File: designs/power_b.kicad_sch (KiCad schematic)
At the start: 30 parts, among them J10 1P2, J11 1P0, J12 GND, J7 3P3, J8 1P8, J9 1P0, U3 TPS82085SIL, U4 MAX1589AETT100T, U5 MIC47050-1.2YML, U6 TPS82085SIL

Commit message: Add files via upload
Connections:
- net +3V3: no longer C52.1, U3.1 (EN), U3.3 (VIN), U3.4 (VIN)
- new net: C52.1, U3.1 (EN), U3.3 (VIN), U3.4 (VIN)
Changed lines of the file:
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@@
 		(lib_id "PicoEVB-rescue:CP")
 		(at 215.9 43.18 0)
+		(mirror y)
 		(unit 1)
 		(exclude_from_sim no)
@@
 		(dnp no)
 		(property "Reference" "C62"
-			(at 216.535 40.64 0)
+			(at 215.265 40.64 0)
 			(effects
 				(font
@@
 		)
 		(property "Value" "100uf"
-			(at 216.535 45.72 0)
+			(at 215.265 45.72 0)
 			(effects
 				(font
@@
 		)
 		(property "Footprint" "fp_archive:C_0805"
-			(at 216.8652 46.99 0)
+			(at 214.9348 46.99 0)
 			(effects
 				(font

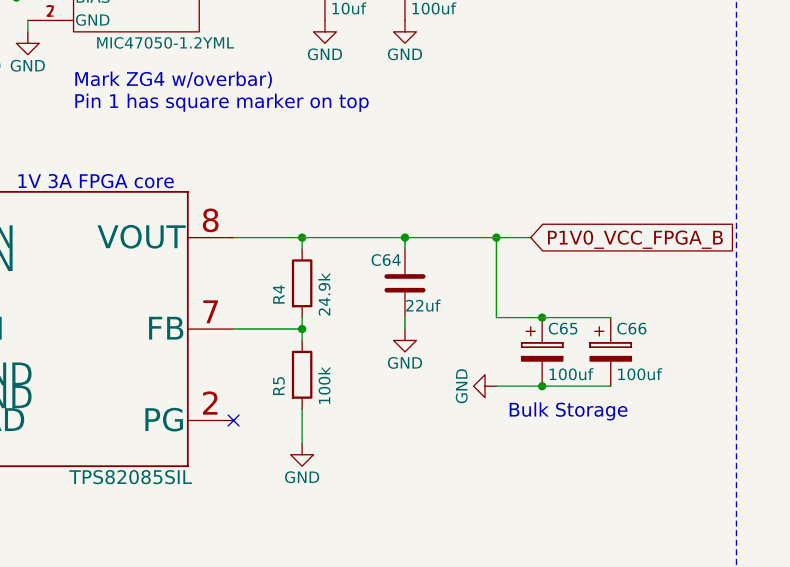
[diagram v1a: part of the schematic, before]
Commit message: Finished 3V3 filled zone wiring for all ICs
IO yet to be wired.
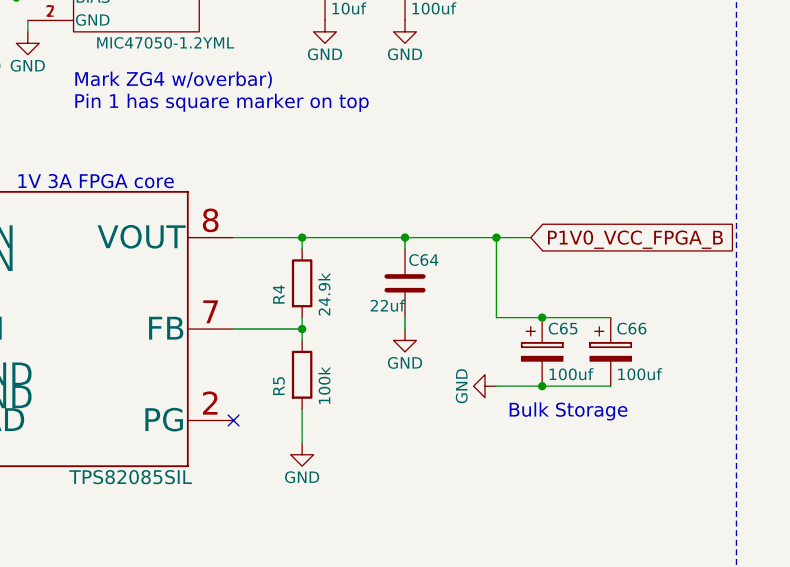
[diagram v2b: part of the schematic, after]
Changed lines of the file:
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@@
 		(lib_id "PicoEVB-rescue:C")
 		(at 217.17 96.52 0)
+		(mirror y)
 		(unit 1)
 		(exclude_from_sim no)
@@
 		(dnp no)
 		(property "Reference" "C64"
-			(at 213.36 93.98 0)
+			(at 220.98 93.98 0)
 			(effects
 				(font
@@
 		)
 		(property "Footprint" "fp_archive:C_0603"
-			(at 218.1352 100.33 0)
+			(at 216.2048 100.33 0)
 			(effects
 				(font
